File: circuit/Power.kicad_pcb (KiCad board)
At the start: 2 copper layers, 100 x 100 mm, 82 parts, among them Q1 IRF530NPbF, Q2 BC547, Q3 BC557, Q4 BC547, U1 74AC164, U10 74AC164, U11 CSR8635_MODULE, U12 TPA3136D2, U13 CSR_DebugSmall, U2 DS18B20, U5 AVR-ISP6, U6 ATMEGA8-16AU, U7 74AC164, U8 DBG, U9 LM2576T-ADJ, Y1 16MHz

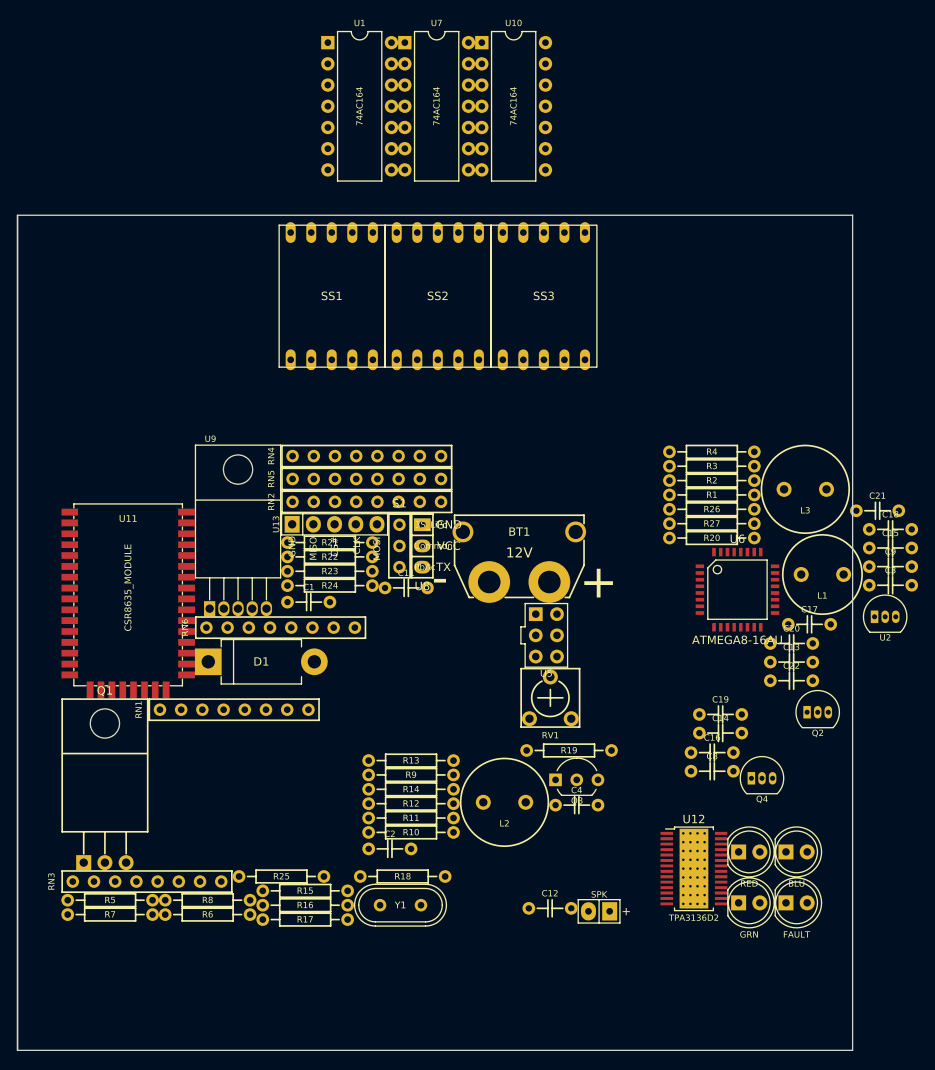
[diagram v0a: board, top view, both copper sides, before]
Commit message: PCB layout started - still need to move the amp and surrounding components
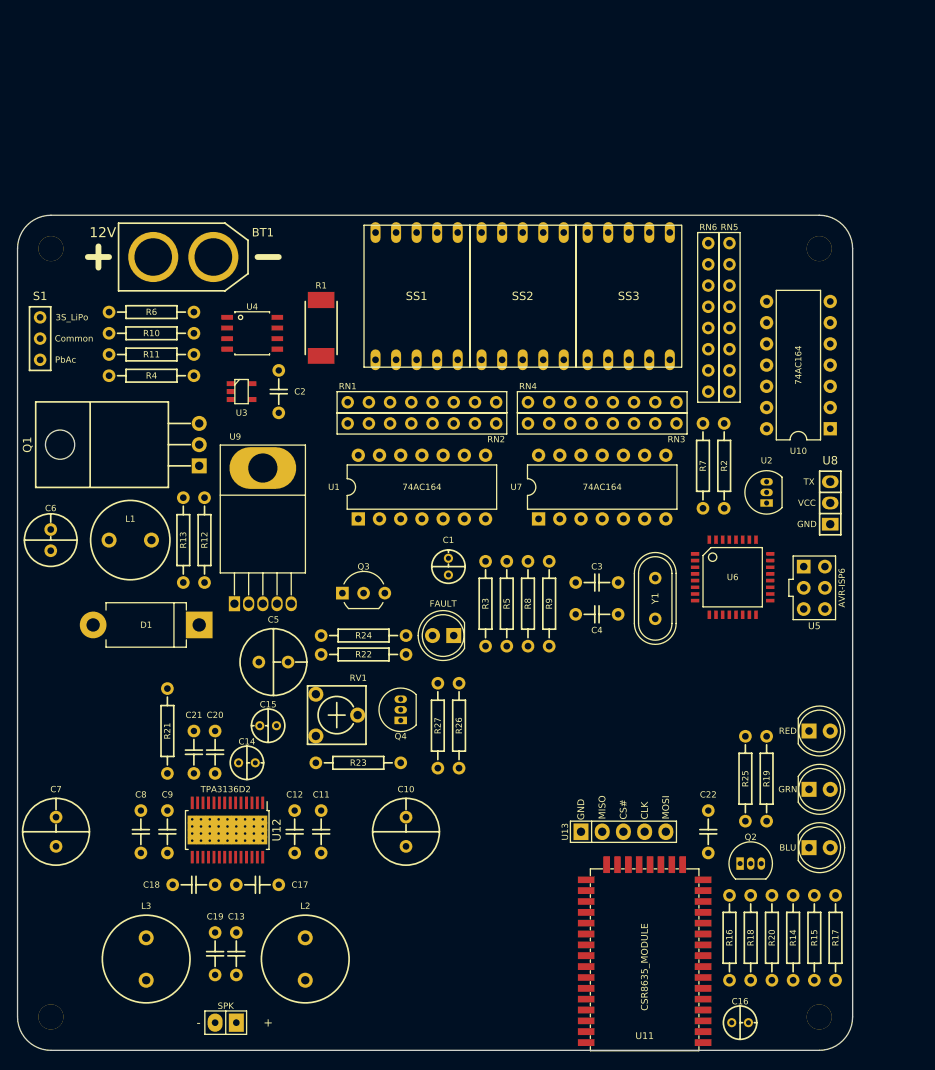
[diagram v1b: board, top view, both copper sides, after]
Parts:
- added C10: 220uF, NovaBox:CPOL_D8_P3.5, F.Cu at (96.5, 123.8)
- added C5: 100uF, NovaBox:CPOL_D8_P3.5, F.Cu at (80.6, 103.5)
- added C6: 100uF, NovaBox:CPOL_D6.3_P2.5, F.Cu at (54.0, 88.9)
- added C7: 220uF, NovaBox:CPOL_D8_P3.5, F.Cu at (54.6, 123.8)
- added J1: HOLE, NovaBox:MountingHole, F.Cu at (54.0, 54.0)
- added J2: HOLE, NovaBox:MountingHole, F.Cu at (54.0, 146.0)
- added J3: HOLE, NovaBox:MountingHole, F.Cu at (146.0, 54.0)
- added J4: HOLE, NovaBox:MountingHole, F.Cu at (146.0, 146.0)
- added U3: MAX6457, NovaBox:SOT-23-5, F.Cu at (76.8, 71.1)
- added U4: INA219_SOIC, NovaBox:SOIC-8_3.9x4.9mm_Pitch1.27mm, F.Cu at (78.1, 64.1)
- BT1: footprint NovaBox:XT60PW-M -> NovaBox:XT60-M
- C1, C14, C15, C16: footprint NovaBox:C_5MM -> NovaBox:CPOL_D4_P2
- R1: value 0.2R -> 0.075R; footprint NovaBox:R_10MM -> NovaBox:R_2512
- moved L3 96.9 mm to (65.4, 139.1), turned to 270 degrees
- moved C18 93.6 mm to (71.1, 130.2), turned to 180 degrees
- moved C9 92.2 mm to (67.9, 123.8), turned to 90 degrees
- moved R7 89.0 mm to (132.1, 80.0), turned to 90 degrees
- moved C21 86.8 mm to (71.1, 114.3), turned to 90 degrees
- moved L1 83.0 mm to (63.5, 88.9), turned to 180 degrees
- moved C15 77.5 mm to (80.0, 111.1), turned to 180 degrees
- moved RN3 77.3 mm to (120.0, 74.9)
- moved C13 75.1 mm to (76.2, 138.4), turned to 270 degrees
- moved C17 73.1 mm to (78.7, 130.2)
- moved R6 72.5 mm to (66.0, 61.6)
- moved C20 70.2 mm to (73.7, 114.3), turned to 90 degrees
- moved C8 68.8 mm to (64.8, 123.8), turned to 90 degrees
- moved R4 67.7 mm to (66.0, 69.2), turned to 180 degrees
- moved R10 67.4 mm to (66.0, 64.1)
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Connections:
- net Net-(Q1-Pad1) renamed /SW_GATE
- net Net-(Q2-Pad1) renamed /MFB
- net Net-(R6-Pad2) renamed /MAX_VDIV
- SS1 pad 1: Net-(RN2-Pad2) -> Net-(RN1-Pad2)
- SS1 pad 10: Net-(RN2-Pad6) -> Net-(RN2-Pad8)
- SS1 pad 2: Net-(RN1-Pad8) -> Net-(RN1-Pad4)
- SS1 pad 5: Net-(RN2-Pad8) -> Net-(RN1-Pad8)
- SS1 pad 6: Net-(RN1-Pad4) -> Net-(RN2-Pad2)
- SS1 pad 7: Net-(RN1-Pad2) -> Net-(RN2-Pad4)
- SS1 pad 9: Net-(RN2-Pad4) -> Net-(RN2-Pad6)
- SS2 pad 1: Net-(RN4-Pad2) -> Net-(RN3-Pad2)
- SS2 pad 10: Net-(RN4-Pad6) -> Net-(RN4-Pad8)
- SS2 pad 2: Net-(RN3-Pad8) -> Net-(RN3-Pad4)
- SS2 pad 5: Net-(RN4-Pad8) -> Net-(RN3-Pad8)
- SS2 pad 6: Net-(RN3-Pad4) -> Net-(RN4-Pad2)
- SS2 pad 7: Net-(RN3-Pad2) -> Net-(RN4-Pad4)
- SS2 pad 9: Net-(RN4-Pad4) -> Net-(RN4-Pad6)
- SS3 pad 1: Net-(RN6-Pad2) -> Net-(RN5-Pad2)
- SS3 pad 10: Net-(RN6-Pad6) -> Net-(RN6-Pad8)
- SS3 pad 2: Net-(RN5-Pad8) -> Net-(RN5-Pad4)
- SS3 pad 5: Net-(RN6-Pad8) -> Net-(RN5-Pad8)
- SS3 pad 6: Net-(RN5-Pad4) -> Net-(RN6-Pad2)
- SS3 pad 7: Net-(RN5-Pad2) -> Net-(RN6-Pad4)
- SS3 pad 9: Net-(RN6-Pad4) -> Net-(RN6-Pad6)
- U1 pad 14: VCC -> +4V
- U10 pad 14: VCC -> +4V
- U6 pad 12: DS18_DQ -> (no net)
- U6 pad 2: AMP_SHDN -> (no net)
- U6 pad 25: (no net) -> DS18_DQ
- U6 pad 9: (no net) -> AMP_SHDN
- U7 pad 14: VCC -> +4V
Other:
- outline, holes or cut-outs redrawn
- net class Default: clearance 0.2 -> 0.2032; trace_width 0.25 -> 0.2032
- rule trace_clearance: 0.2 -> 0.2032

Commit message: routing!
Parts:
- C10, C7: value 220uF -> 220μF
- C11, C12, C13, C17, C18, C19, C20, C21, C8, C9: footprint NovaBox:C_5MM -> NovaBox:C_1206
- C14, C15, C16: footprint NovaBox:CPOL_D4_P2 -> NovaBox:C_1206
- C3, C4: footprint NovaBox:C_5MM -> NovaBox:C_2.5MM
- C5, C6: value 100uF -> 100μF
- L1: value 680uH -> 680μH
- L2, L3: value 10uH -> 10μH
- moved C7 38.8 mm to (87.6, 103.5), turned to 0 degrees
- moved R24 38.7 mm to (128.9, 109.9), turned to 90 degrees
- moved R22 33.2 mm to (123.8, 109.9), turned to 90 degrees
- moved S2 31.7 mm to (53.7, 123.2), turned to 270 degrees
- moved R27 31.1 mm to (131.4, 109.9), turned to 270 degrees
- moved Q3 29.1 mm to (118.7, 105.4), turned to 90 degrees
- moved RV1 28.2 mm to (102.2, 132.7), turned to 90 degrees
- moved C6 27.1 mm to (79.4, 79.4), turned to 180 degrees
- moved L2 27.0 mm to (58.4, 132.1), turned to 180 degrees
- moved L3 25.7 mm to (58.4, 114.3), turned to 180 degrees
- moved R26 23.5 mm to (126.4, 109.9), turned to 270 degrees
- moved Q4 23.4 mm to (118.7, 114.3)
- moved C21 23.2 mm to (93.7, 119.4), turned to 0 degrees
- moved C10 22.8 mm to (87.6, 144.8), turned to 0 degrees
- moved R21 22.3 mm to (90.2, 113.7), turned to 180 degrees
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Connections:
- C20 pad 2: SPK_RN -> SPK_RP
- C21 pad 2: SPK_RP -> SPK_RN
- SS3 pad 3: (no net) -> GND
- SS3 pad 8: (no net) -> GND
- U5 pad 3: LED_CK -> Net-(U5-Pad3)
- U5 pad 4: LED_DT -> Net-(U5-Pad4)
- U6 pad 1: (no net) -> LED_RST
- U6 pad 11: LED_RST -> (no net)
- U6 pad 15: LED_DT -> Net-(U5-Pad4)
- U6 pad 17: LED_CK -> Net-(U5-Pad3)
- U6 pad 30: (no net) -> LED_DT
- U6 pad 32: (no net) -> LED_CK
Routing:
- net +4V: track 0.00 -> 263.9 mm, vias 0 -> 1
- net VDD: track 0.00 -> 208.8 mm
- net SDA: track 0.00 -> 84.9 mm, vias 0 -> 2
- net SCL: track 0.00 -> 81.0 mm, vias 0 -> 2
- net Net-(RN4-Pad7): track 0.00 -> 63.1 mm
- net LED_CK: track 0.00 -> 62.7 mm, vias 0 -> 1
- net LED_RST: track 0.00 -> 61.5 mm
- net +BATT: track 0.00 -> 55.9 mm
- net Net-(Q4-Pad1): track 0.00 -> 54.7 mm, vias 0 -> 1
- net LED_DT: track 0.00 -> 45.9 mm, vias 0 -> 1
- net -BATT: track 0.00 -> 43.9 mm
- net Net-(RN5-Pad8): track 0.00 -> 40.6 mm
- net SPK_RN: track 0.00 -> 37.2 mm
- net SPK_RP: track 0.00 -> 36.7 mm
- net LED_B: track 0.00 -> 34.3 mm, vias 0 -> 1
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- added copper zone on B.Cu, net GND
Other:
- rule trace_min: 0.2 -> 0.2032

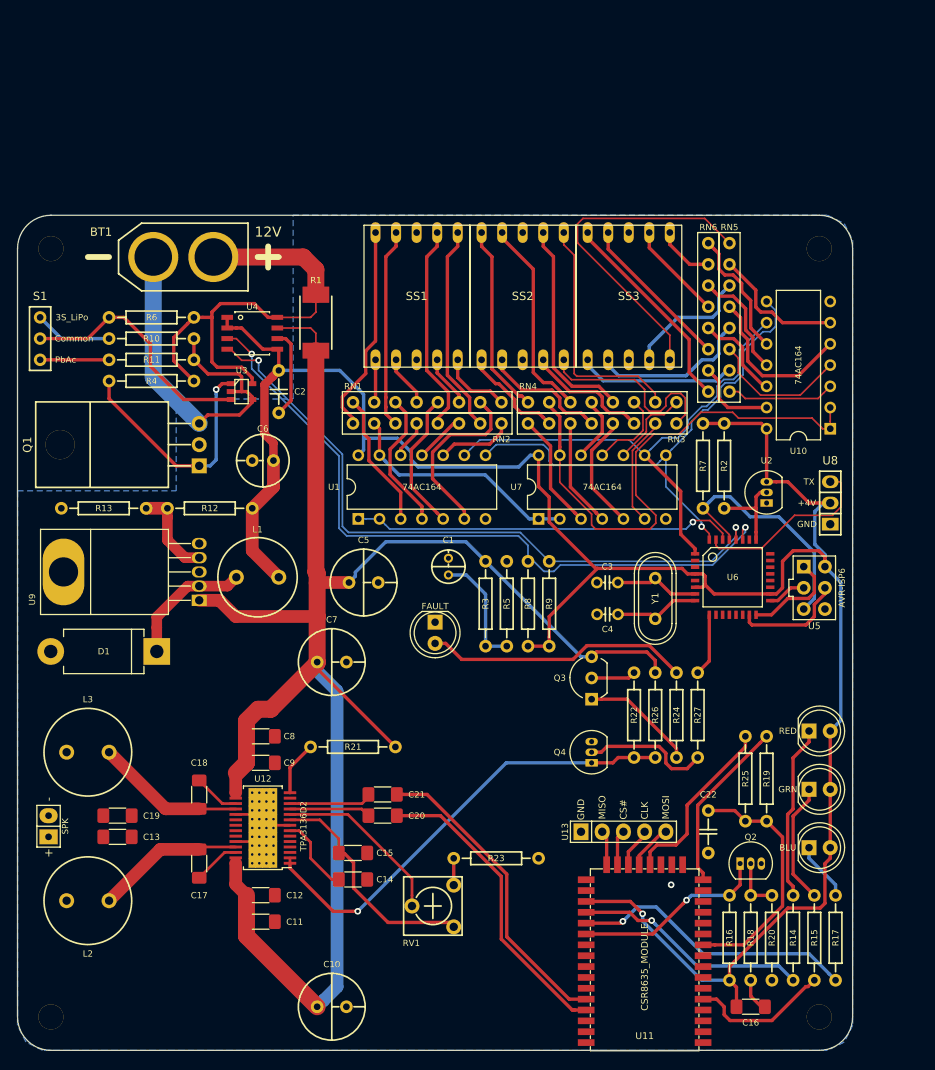
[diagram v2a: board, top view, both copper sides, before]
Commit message: first version of routing done, but needs lots of improvements
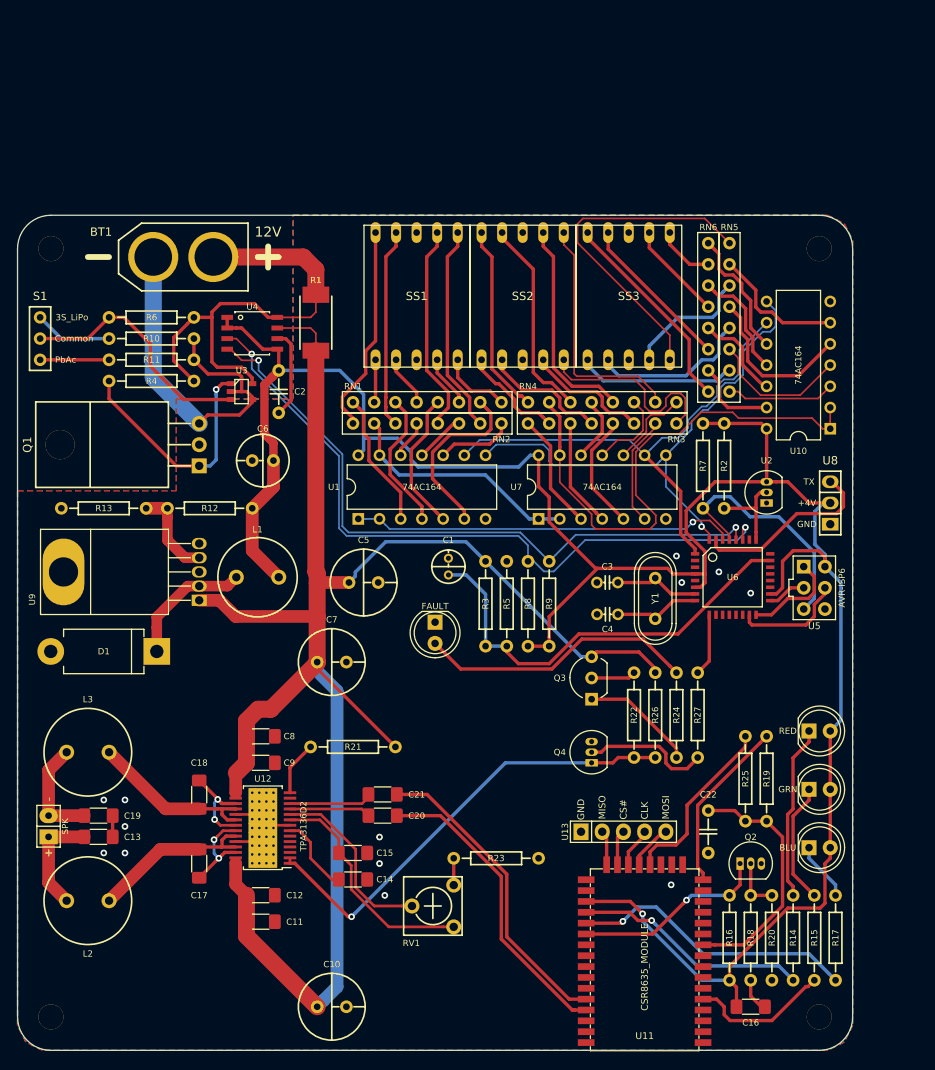
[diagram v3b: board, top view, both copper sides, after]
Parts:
- moved C13 2.28 mm to (59.7, 124.4)
- moved C19 2.28 mm to (59.7, 121.9)
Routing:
- net BATT_SNS: track 14.2 -> 52.1 mm
- net Net-(C13-Pad2): track 0.00 -> 12.8 mm
- net Net-(C19-Pad2): track 0.00 -> 12.8 mm
- net +4V: track 263.9 -> 275.2 mm
- net Net-(C17-Pad2): track 5.63 -> 11.1 mm, vias 0 -> 2
- net Net-(C18-Pad2): track 5.52 -> 10.9 mm, vias 0 -> 2
- net Net-(C17-Pad1): track 17.8 -> 20.5 mm
- net Net-(C18-Pad1): track 18.0 -> 20.6 mm
- net GND: track 19.8 -> 22.3 mm, vias 1 -> 13
- net Net-(D5-Pad2): track 31.7 -> 33.3 mm
- net Net-(RV1-Pad2): track 21.1 -> 21.8 mm
- net SCL: track 81.0 -> 80.4 mm
- net VDD: track 208.8 -> 208.3 mm
- added copper zone on F.Cu, net GND

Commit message: White boy alpha!
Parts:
- added T1: PB0, NovaBox:TestPad, F.Cu at (134.6, 101.0)
- added T2: PB1, NovaBox:TestPad, F.Cu at (136.5, 104.1)
- added T3: PB2, NovaBox:TestPad, F.Cu at (138.4, 101.0)
- added T4: PC1, NovaBox:TestPad, F.Cu at (142.2, 88.9)
- added T5: PC3, NovaBox:TestPad, F.Cu at (137.0, 84.6)
- added T6: PD6, NovaBox:TestPad, F.Cu at (131.8, 100.2)
- added T7: PD7, NovaBox:TestPad, F.Cu at (132.3, 102.7)
- S2: footprint NovaBox:SPKR -> NovaBox:SPKR_BIG
- moved C13 3.18 mm to (62.9, 124.5)
- moved C19 3.18 mm to (62.9, 121.9)
- moved U2 2.54 mm to (139.7, 80.6)
- moved L2 2.54 mm to (61.0, 132.1)
- moved L3 2.54 mm to (61.0, 114.3)
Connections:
- U6 pad 10: (no net) -> Net-(T6-Pad1)
- U6 pad 11: (no net) -> Net-(T7-Pad1)
- U6 pad 12: (no net) -> Net-(T1-Pad1)
- U6 pad 13: (no net) -> Net-(T2-Pad1)
- U6 pad 14: (no net) -> Net-(T3-Pad1)
- U6 pad 20: (no net) -> +4V
- U6 pad 24: (no net) -> Net-(T4-Pad1)
- U6 pad 26: (no net) -> Net-(T5-Pad1)
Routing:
- net Net-(RN5-Pad8): track 40.6 -> 25.1 mm
- net DS18_DQ: track 10.4 -> 17.1 mm
- net Net-(T2-Pad1): track 0.00 -> 6.50 mm
- net Net-(T7-Pad1): track 0.00 -> 5.73 mm
- net Net-(T5-Pad1): track 0.00 -> 4.75 mm
- net Net-(C19-Pad2): track 12.8 -> 16.7 mm
- net Net-(C13-Pad2): track 12.8 -> 16.8 mm
- net Net-(T3-Pad1): track 0.00 -> 3.78 mm
- net Net-(T1-Pad1): track 0.00 -> 3.38 mm
- net Net-(T6-Pad1): track 0.00 -> 3.11 mm
- net Net-(T4-Pad1): track 0.00 -> 2.79 mm
- net GND: track 22.3 -> 19.8 mm
- net Net-(C17-Pad1): track 20.5 -> 18.0 mm
- net Net-(C18-Pad1): track 20.6 -> 18.0 mm
- net AMP_SHDN: track 7.51 -> 9.78 mm
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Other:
- board text added: "White"
- board text added: "boy"
- board text added: "https://github.com/nodep/NovaBox/ 2018.dec.9"

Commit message: white boy continued
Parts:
- added C23: 1uF, NovaBox:C_1206, F.Cu at (141.5, 86.9)
- moved T4 6.38 mm to (148.6, 89.5)
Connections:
- net Net-(C15-Pad1) renamed /GVDD
- net Net-(RV1-Pad2) renamed /PLIMIT
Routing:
- net Net-(RN4-Pad7): track 63.1 -> 49.1 mm, vias 0 -> 1
- net Net-(T4-Pad1): track 2.79 -> 12.9 mm
- net +4V: track 275.7 -> 282.0 mm
- net Net-(Q4-Pad1): track 54.9 -> 57.0 mm
- net Net-(U6-Pad31): track 22.2 -> 23.8 mm
- net Net-(RN5-Pad7): track 16.1 -> 15.0 mm
- net Net-(RN4-Pad2): track 29.2 -> 28.1 mm
- net AMP_SHDN: track 9.78 -> 8.80 mm
- net Net-(R21-Pad2): track 6.50 -> 7.27 mm
- net Net-(RN3-Pad8): track 24.3 -> 23.7 mm
- net GND: vias 13 -> 19
